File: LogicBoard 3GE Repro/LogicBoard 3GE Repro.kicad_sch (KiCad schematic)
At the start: 161 parts, among them IC201 27C512PLCC, IC204 CY62256-70PC, IC206 MC6809E, IC207 6522, IC208 YM2149, IC209 74HC74, IC301 MC1408, IC302 CD4052B, IC303 LF347, IC304 LF353, IC305 4066, J201 CART, J202 DB9_Male, J203 DB9_Male, J204 Power, J301 Video, J302 Audio, Q301 2N3905, Q302 2N3905, Q303 2N3904, SW201 Reset, U1 ATF16V8Bxx-xxPU

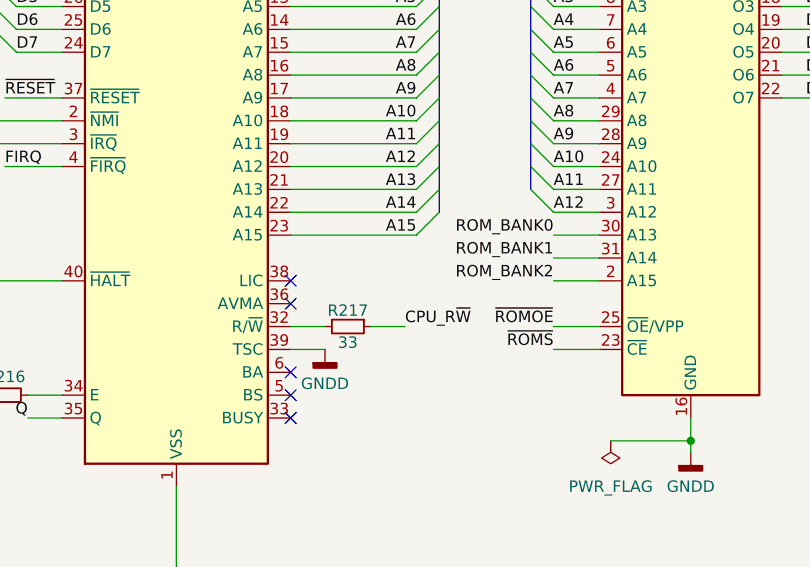
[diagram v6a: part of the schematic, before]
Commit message: Repro: name CPU_R/W net (fix R217 short) - Phase 1 schematic clean
CPU_R~W = IC206.32 + R217.2; R~W = R217.1 + VIA/cart/GAL. R217 series
resistor correctly between CPU and bus R/W. ERC 11 (all intentional/trivial).

Co-Authored-By: Claude Opus 4.8 <noreply@anthropic.com>
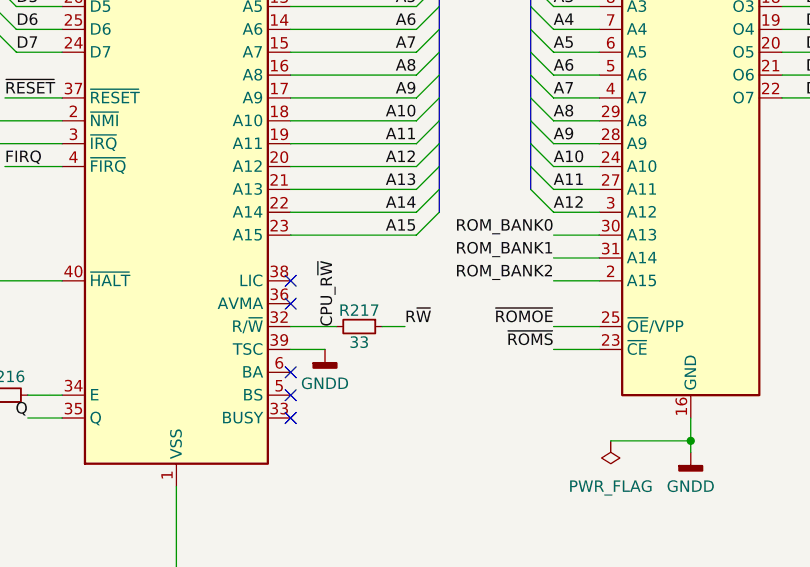
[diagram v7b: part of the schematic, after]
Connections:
- net CPU_R~{W}: now also IC206.32 (R/~{W}), R217.2; no longer R217.1
- net R~{W}: now also R217.1
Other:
- moved on the sheet: R217
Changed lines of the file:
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@@
 	(wire
 		(pts
-			(xy 123.19 86.36) (xy 127 86.36)
-		)
-		(stroke
-			(width 0)
-			(type default)
-		)
-	)
-	(wire
-		(pts
 			(xy 173.99 45.72) (xy 168.91 45.72)
 		)
@@
 	(wire
 		(pts
-			(xy 114.3 86.36) (xy 118.11 86.36)
+			(xy 114.3 86.36) (xy 119.38 86.36)
 		)
 		(stroke
@@
 	(wire
 		(pts
+			(xy 124.46 86.36) (xy 127 86.36)
+		)
+		(stroke
+			(width 0)
+			(type default)
+		)
+	)
+	(wire
+		(pts
 			(xy 289.56 163.83) (xy 312.42 163.83)
 		)
@@
 		)
 	)
-	(label "CPU_R~{W}"
+	(label "R~{W}"
 		(at 127 86.36 0)
 		(effects
@@
 		)
 	)
+	(label "CPU_R~{W}"
+		(at 119.38 86.36 90)
+		(effects
+			(font
+				(size 1.27 1.27)
+			)
+			(justify left bottom)
+		)
+	)
 	(label "D7"
 		(at 224.79 57.15 180)
@@
 	(symbol
 		(lib_id "Device:R_Small")
-		(at 120.65 86.36 270)
+		(at 121.92 86.36 270)
 		(unit 1)
 		(body_style 1)
@@
 		(dnp no)
 		(property "Reference" "R217"
-			(at 120.65 84.582 90)
+			(at 121.92 84.582 90)
 			(show_name no)
 			(do_not_autoplace no)
@@
 		)
 		(property "Value" "33"
-			(at 120.65 88.138 90)
+			(at 121.92 88.138 90)
 			(show_name no)
 			(do_not_autoplace no)
@@
 		)
 		(property "Footprint" "Vectrex LogicBoard:R_Axial_DIN0207_L6.3mm_D2.5mm_P12.70mm_Horizontal"
-			(at 120.65 86.36 0)
+			(at 121.92 86.36 0)
 			(hide yes)
 			(show_name no)
@@
 		)
 		(property "Datasheet" ""
-			(at 120.65 86.36 0)
+			(at 121.92 86.36 0)
 			(hide yes)
 			(show_name no)
@@
 		)
 		(property "Description" "Resistor, small symbol"
-			(at 120.65 86.36 0)
+			(at 121.92 86.36 0)
 			(hide yes)
 			(show_name no)
@@
 		)
 		(property "Mouser" "603-CFR-25JR-5233R"
-			(at 46.99 -30.48 0)
+			(at 48.26 -30.48 0)
 			(hide yes)
 			(show_name no)

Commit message: Repro Phase 2: passive footprints (SMD 0402) + integrator caps fixed
All R/C/FB footprints assigned (0402 passives, larger caps sized). Integrator
caps C304/305/306->4.7nF, C312/313=10nF, all C_0603 C0G (3GE rev, styrene->C0G).
FB201/202->L_0805. ERC 11 (all intentional/trivial).

Co-Authored-By: Claude Opus 4.8 <noreply@anthropic.com>
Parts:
- C1, C2: value 0.1uf -> 0.1uF; footprint (none) -> Capacitor_SMD:C_0402_1005Metric
- C201, C202, C203, C204, C206, C207, C208, C209, C214, C215, C216, C217, C218, C219, C220, C221, C223, C224, C229, C230, C231, C232, C233, C234, C235, C236, C237, C239, C301, C302, C303, C307, C308, C309, C310, C311, C314, C315, C316, C317, C320, C321, C324, C325, C326, C327, C328: footprint Capacitor_THT:C_Disc_D5.0mm_W2.5mm_P5.00mm -> Capacitor_SMD:C_0402_1005Metric
- C211: footprint Capacitor_THT:CP_Radial_D8.0mm_P2.50mm -> Capacitor_SMD:CP_Elec_8x10.5
- C212, C213: footprint Capacitor_THT:CP_Radial_D8.0mm_P2.50mm -> Capacitor_SMD:CP_Elec_6.3x7.7
- C227: footprint Capacitor_THT:CP_Radial_Tantal_D5.5mm_P2.50mm -> Capacitor_SMD:C_1206_3216Metric
- C228: footprint Capacitor_THT:CP_Radial_Tantal_D5.0mm_P2.50mm -> Capacitor_SMD:C_1206_3216Metric
- C304, C305, C306: value 10nF -> 4.7nF C0G; footprint Capacitor_THT:C_Disc_D7.5mm_W5.0mm_P5.00mm -> Capacitor_SMD:C_0603_1608Metric
- C312, C313: value 10nF -> 10nF C0G; footprint Capacitor_THT:C_Disc_D7.5mm_W5.0mm_P5.00mm -> Capacitor_SMD:C_0603_1608Metric
- C323: footprint Capacitor_THT:CP_Radial_D4.0mm_P2.00mm -> Capacitor_SMD:C_0805_2012Metric
- D201, D301, D302: footprint Diode_THT:D_DO-34_SOD68_P12.70mm_Horizontal -> (none)
- FB201, FB202: footprint Inductor_THT:L_Axial_L7.0mm_D3.3mm_P12.70mm_Horizontal_Fastron_MICC -> Inductor_SMD:L_0805_2012Metric
- IC201: footprint Package_LCC:PLCC-32_11.4x14.0mm_P1.27mm -> (none)
- IC204: footprint Package_DIP:DIP-28_W15.24mm -> (none)
- IC206, IC207, IC208: footprint Package_DIP:DIP-40_W15.24mm -> (none)
- IC301, IC302: footprint Package_DIP:DIP-16_W7.62mm -> (none)
- IC303, IC305: footprint Package_DIP:DIP-14_W7.62mm -> (none)
- IC304: footprint Package_DIP:DIP-8_W7.62mm -> (none)
- J201: footprint Vectrex LogicBoard:SULLINS_EBC18DRAS -> (none)
- OSC1: footprint Oscillator:Oscillator_SMD_EuroQuartz_XO32-4Pin_3.2x2.5mm -> (none)
- Q301, Q302, Q303: footprint Package_TO_SOT_THT:TO-92_Inline -> (none)
- R201, R202, R203, R204, R205, R206, R207, R208, R214, R215, R216, R217, R218, R219, R220, R221, R222, R223, R224, R225, R301, R303, R304, R305, R306, R307, R308, R309, R310, R311, R312, R313, R314, R315, R316, R317, R318, R319, R320, R321, R322, R323, R324, R325, R327, R329, R330, R332, R334, R336, R338, R339, R340, R341, R342, R343, R344, R345, R346: footprint Vectrex LogicBoard:R_Axial_DIN0207_L6.3mm_D2.5mm_P12.70mm_Horizontal -> Resistor_SMD:R_0402_1005Metric
- R302, R333, R335: footprint Potentiometer_THT:Potentiometer_ACP_CA14-H5_Horizontal -> Resistor_SMD:R_0402_1005Metric
- R326: footprint Vectrex LogicBoard:Potentiometer_UndLab_Horizontal -> Resistor_SMD:R_0402_1005Metric
- SW201: footprint TestPoint:TestPoint_Bridge_Pitch5.08mm_Drill1.3mm -> (none)
- U1: footprint Package_DIP:DIP-20_W7.62mm -> (none)
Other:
- note added: "JUMPERS"
